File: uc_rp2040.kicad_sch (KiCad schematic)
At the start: 44 parts, among them Q2 BSS138PW, Q6 BC817-25W, SW2 SW_B3U-1000P_SMD, SW3 SW_B3U-1000P_SMD, U8 W25Q128JVSIQ_SOIC-8, U9 RP2040, Y1 Oscillator_12MHz_ESC_2520MV

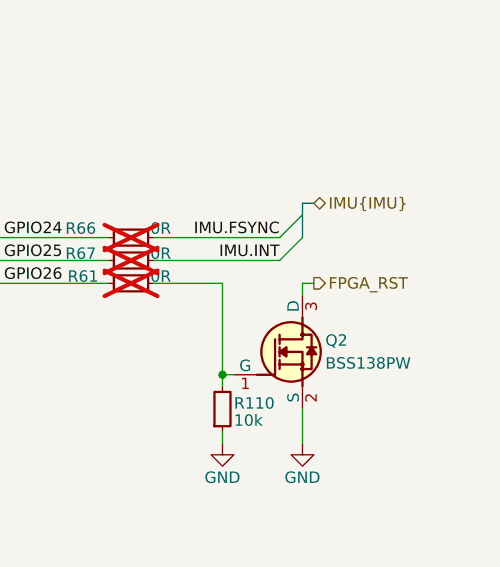
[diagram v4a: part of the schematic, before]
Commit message: [#72133] Clean ERC
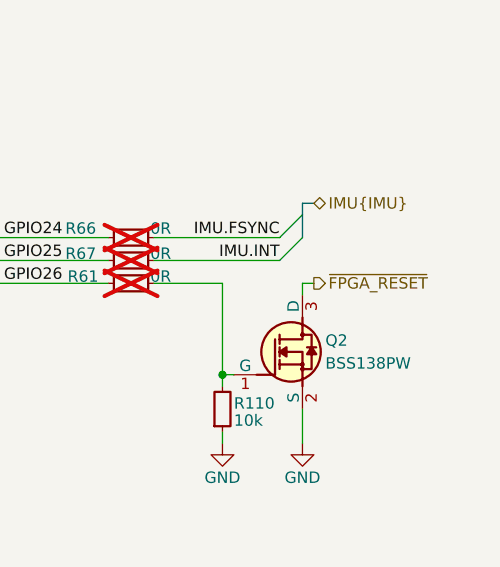
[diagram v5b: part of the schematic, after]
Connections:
- net FPGA_RST renamed ~{FPGA_RESET}
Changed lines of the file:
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@@
 		)
 	)
-	(hierarchical_label "FPGA_RST"
+	(hierarchical_label "~{FPGA_RESET}"
 		(shape output)
 		(at 240.03 125.73 0)

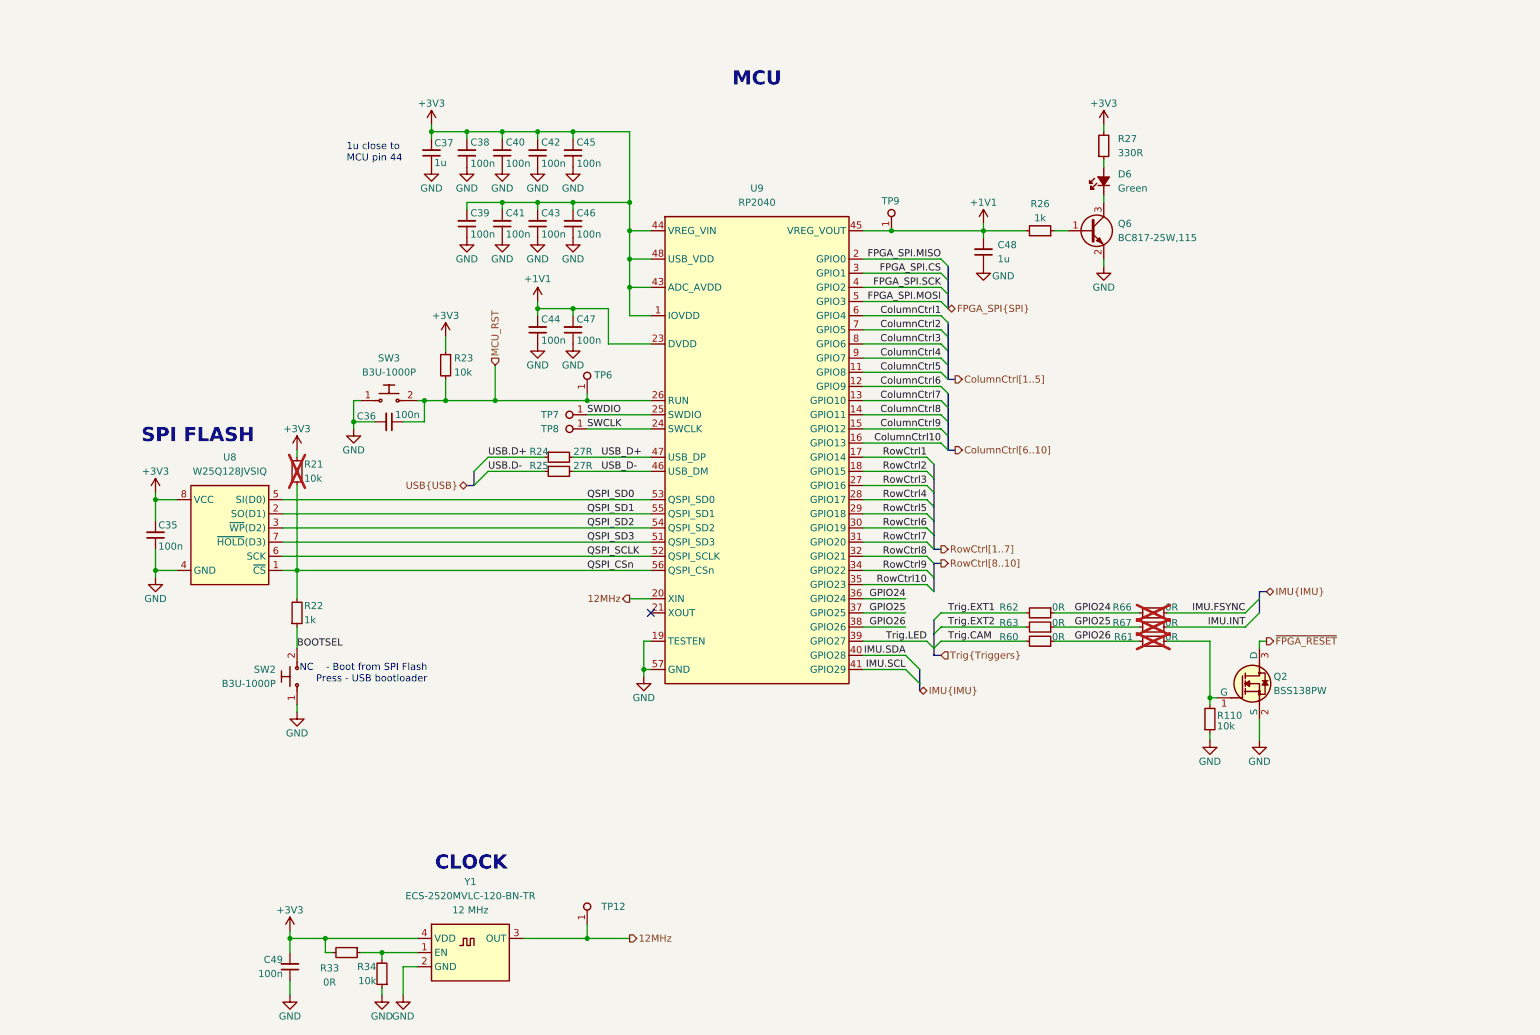
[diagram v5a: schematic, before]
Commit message: [#72447] Update clock & SPI connections
Signed-off-by: Dawid Lentka <dlentka@antmicro.com>
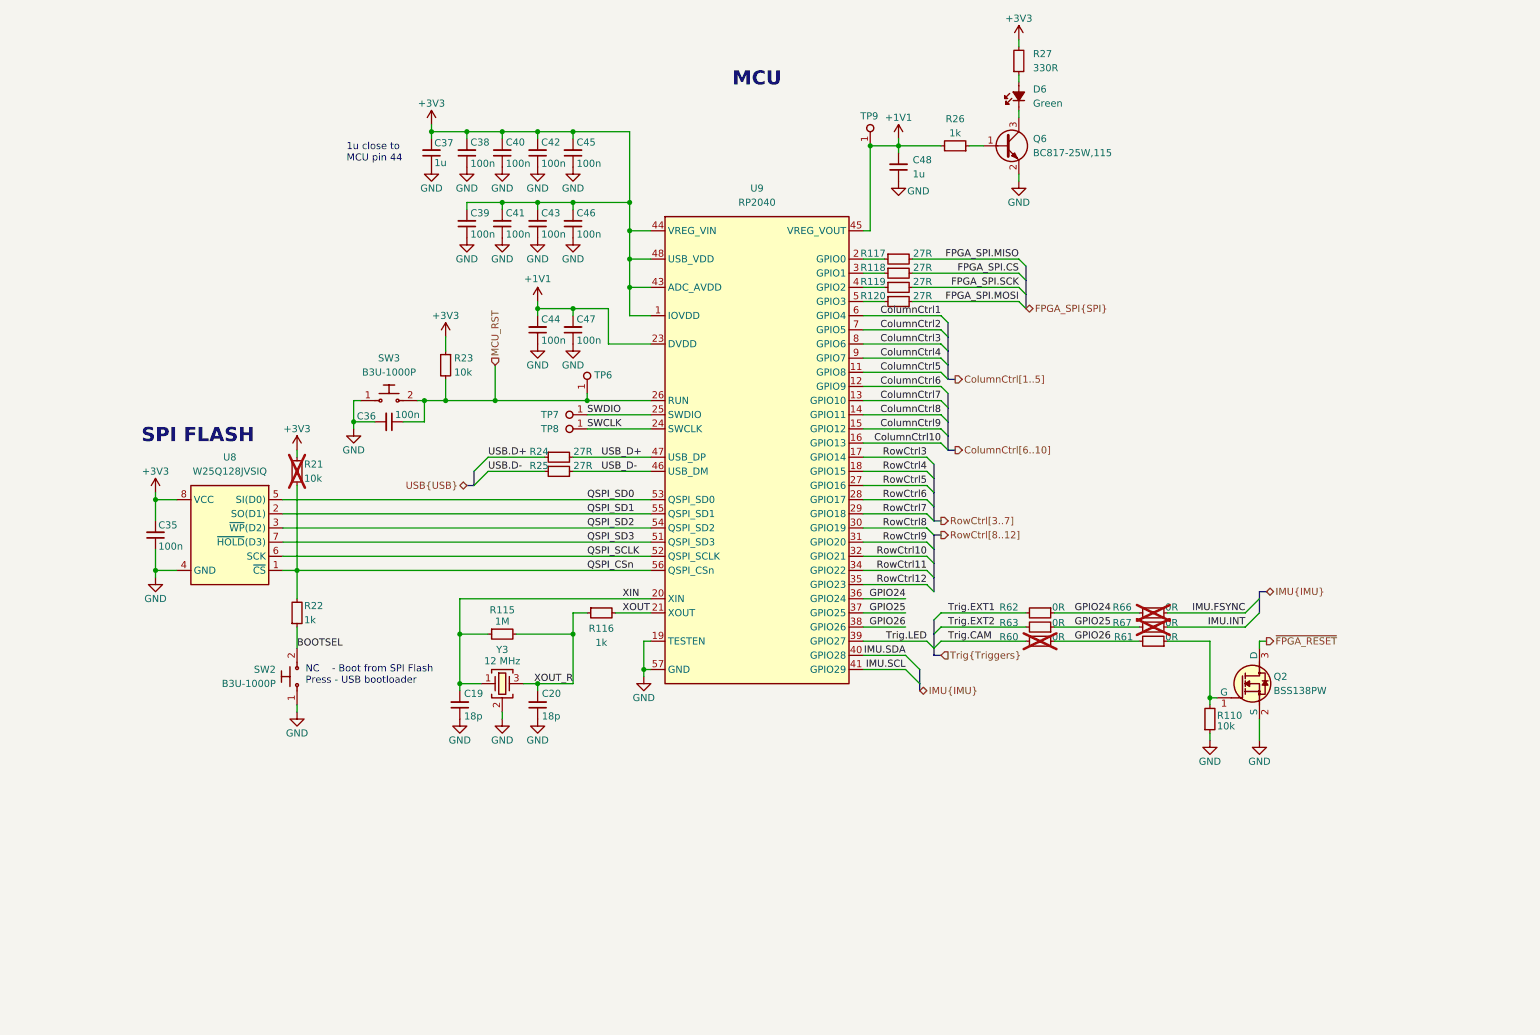
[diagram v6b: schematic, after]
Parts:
- removed C49: C_100n_0402, antmicro-footprints:C_0402_1005Metric, symbol antmicroCapacitors0402:C_100n_0402
- removed R33: R_0R_0402, antmicro-footprints:R_0402_1005Metric, symbol antmicroResistors0402:R_0R_0402
- removed R34: R_10k_0402, antmicro-footprints:R_0402_1005Metric, symbol antmicroResistors0402:R_10k_0402
- removed TP12: TP_0.75mm_SMD, antmicro-footprints:TP_SMD_0.75mm, symbol antmicroTestPoints:TP_0.75mm_SMD
- removed Y1: Oscillator_12MHz_ESC_2520MV, antmicro-footprints:Oscillator_SMD_ECS_2520MV_2.5x2mm, symbol antmicroOscillators:Oscillator_12MHz_ESC_2520MV
- added C19, C20: C_18p_0402, antmicro-footprints:C_0402_1005Metric, symbol antmicroCapacitors0402:C_18p_0402
- added R115: R_1M_0402, antmicro-footprints:R_0402_1005Metric, symbol antmicroResistors0402:R_1M_0402
- added R116: R_1k_0402, antmicro-footprints:R_0402_1005Metric, symbol antmicroResistors0402:R_1k_0402
- added R117, R118, R119, R120: R_27R_0402, antmicro-footprints:R_0402_1005Metric, symbol antmicroResistors0402:R_27R_0402
- added Y3: Resonator_12MHz_ABM8G, antmicro-footprints:Resonator_SMD_Abracon_ABM8G_3.2x2.5mm, symbol antmicroResonators:Resonator_12MHz_ABM8G
- R60: now not fitted
- R61: now fitted
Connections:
- net RowCtrl1 is gone; now on net RowCtrl3: U9.17 (GPIO14)
- net RowCtrl2 is gone; now on net RowCtrl4: U9.18 (GPIO15)
- net FPGA_SPI.CS: now also R118.2; no longer U9.3 (GPIO1)
- net FPGA_SPI.MISO: now also R117.2; no longer U9.2 (GPIO0)
- net FPGA_SPI.MOSI: now also R120.2; no longer U9.5 (GPIO3)
- net FPGA_SPI.SCK: now also R119.2; no longer U9.4 (GPIO2)
- net GND: now also C19.1, C20.1, Y3.2 (SH), Y3.4 (SH)
- net RowCtrl10: now also U9.32 (GPIO21); no longer U9.35 (GPIO23)
- net RowCtrl3: no longer U9.27 (GPIO16)
- net RowCtrl4: no longer U9.28 (GPIO17)
- net RowCtrl5: now also U9.27 (GPIO16); no longer U9.29 (GPIO18)
- net RowCtrl6: now also U9.28 (GPIO17); no longer U9.30 (GPIO19)
- net RowCtrl7: now also U9.29 (GPIO18); no longer U9.31 (GPIO20)
- net RowCtrl8: now also U9.30 (GPIO19); no longer U9.32 (GPIO21)
- net RowCtrl9: now also U9.31 (GPIO20); no longer U9.34 (GPIO22)
- net XOUT: now reaches U9.21 (XOUT)
- net XOUT: now also R116.2
- net 12MHz renamed XIN
- net XIN: now also C19.2, R115.1, Y3.1
- new net: R120.1, U9.5 (GPIO3)
- new net: R118.1, U9.3 (GPIO1)
- new net: R119.1, U9.4 (GPIO2)
- new net: R117.1, U9.2 (GPIO0)
- new net RowCtrl11: U9.34 (GPIO22)
- new net RowCtrl12: U9.35 (GPIO23)
- new net XOUT_R: C20.2, R115.2, R116.1, Y3.3
- no-connect marks 1 -> 0
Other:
- note removed: "CLOCK"
- moved on the sheet: C48, D6, Q6, R26, R27, TP9
